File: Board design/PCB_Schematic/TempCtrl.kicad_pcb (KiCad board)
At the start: 4 copper layers, 80 x 100 mm, 164 parts, among them CON1 BARREL_JACK, IC1 ATMEGA328P-A, P1 233-2977, P2 820-8104, P3 RS485, P4 USB_OTG, P5 ICSP, P6 ADC breakout, SW1 DISABLE_COMMS, SW2 SWITCH_INV, U1 LM7805, U10 INA330, U11 ISO7242, U12 FT232RL, U13 ADS1262, U14 AD8639, U15 DAC8564, U16 AD8639, U17 DAC8564, U18 74LS125, U2 TMA0505S, U3 ADuM7642CRQZ, U4 ISO3088, U5 OPA548, U6 OPA548, U7 OPA548, U8 OPA548, U9 INA330, X1 TSX-3225 X1E0000210013

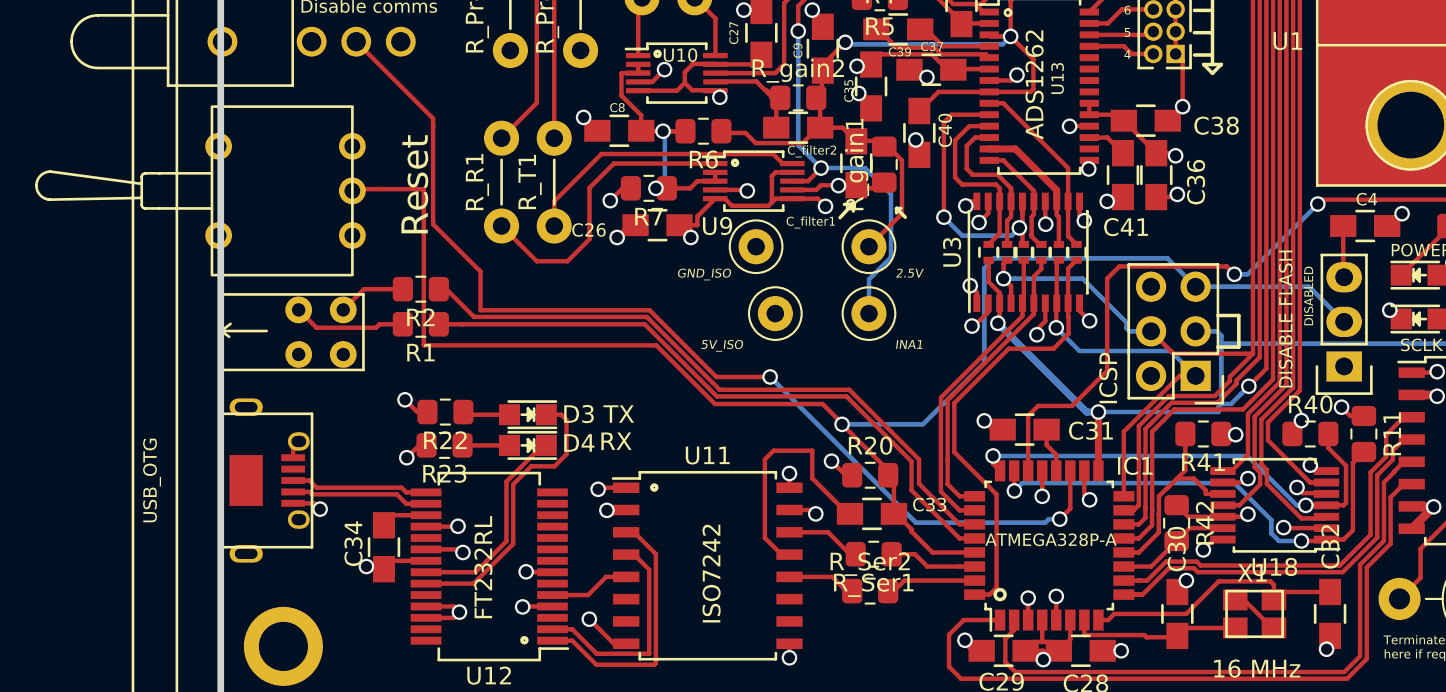
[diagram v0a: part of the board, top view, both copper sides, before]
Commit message: Schematic changes for v5
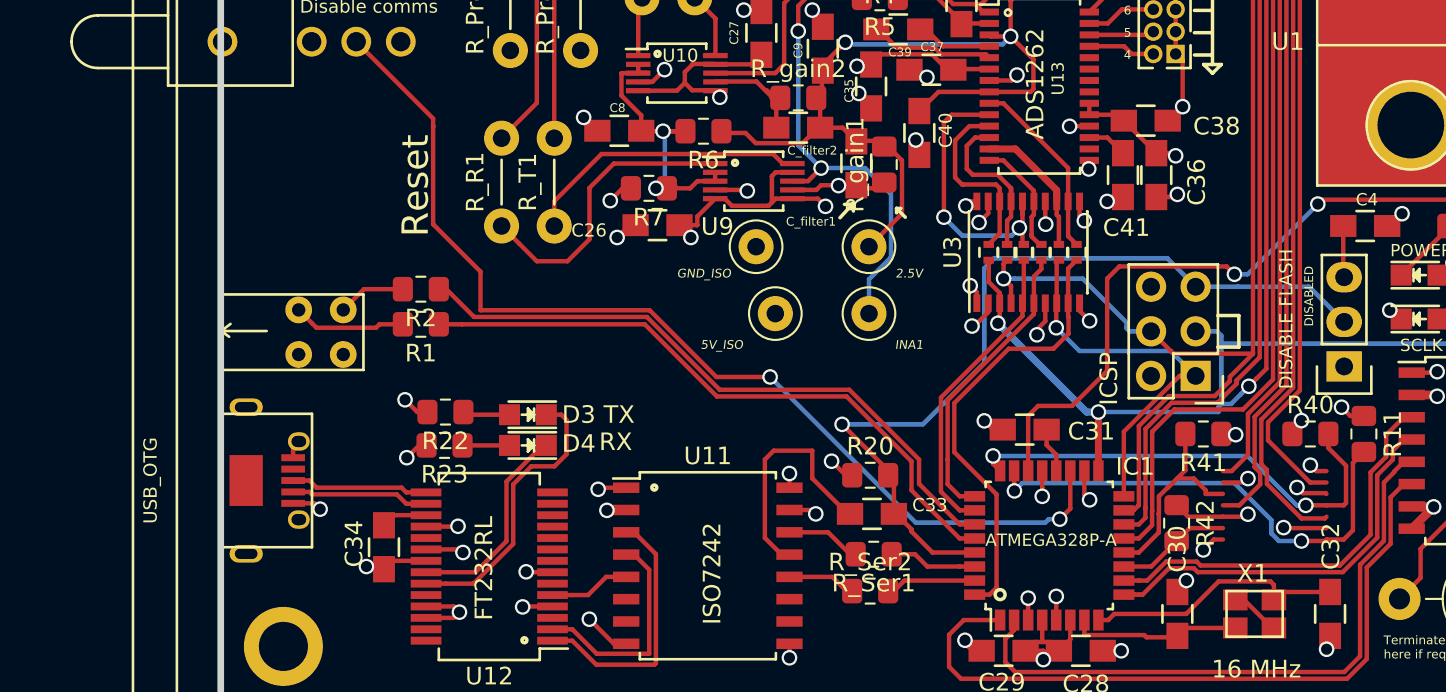
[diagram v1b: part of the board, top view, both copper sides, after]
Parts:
- removed SW2: SWITCH_INV, Custom:Toggle_Switch_819-9385
- removed U18: 74LS125, Package_SO:TSSOP-14_4.4x5mm_P0.65mm
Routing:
- net /ARD_RST: track 87.9 -> 49.1 mm

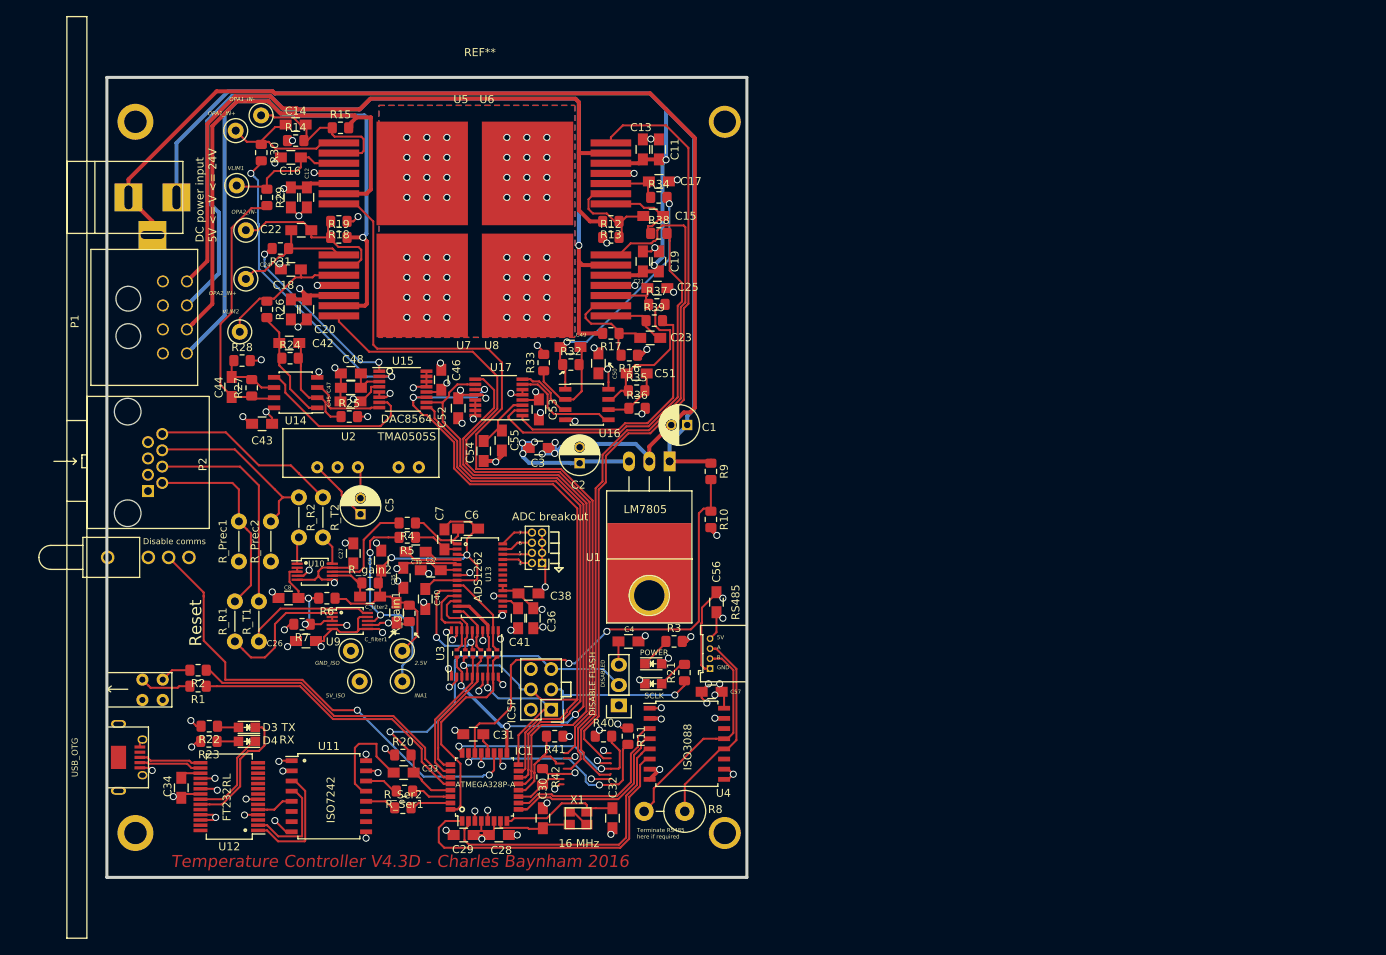
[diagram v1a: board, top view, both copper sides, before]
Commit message: Update schematic with v5 changes
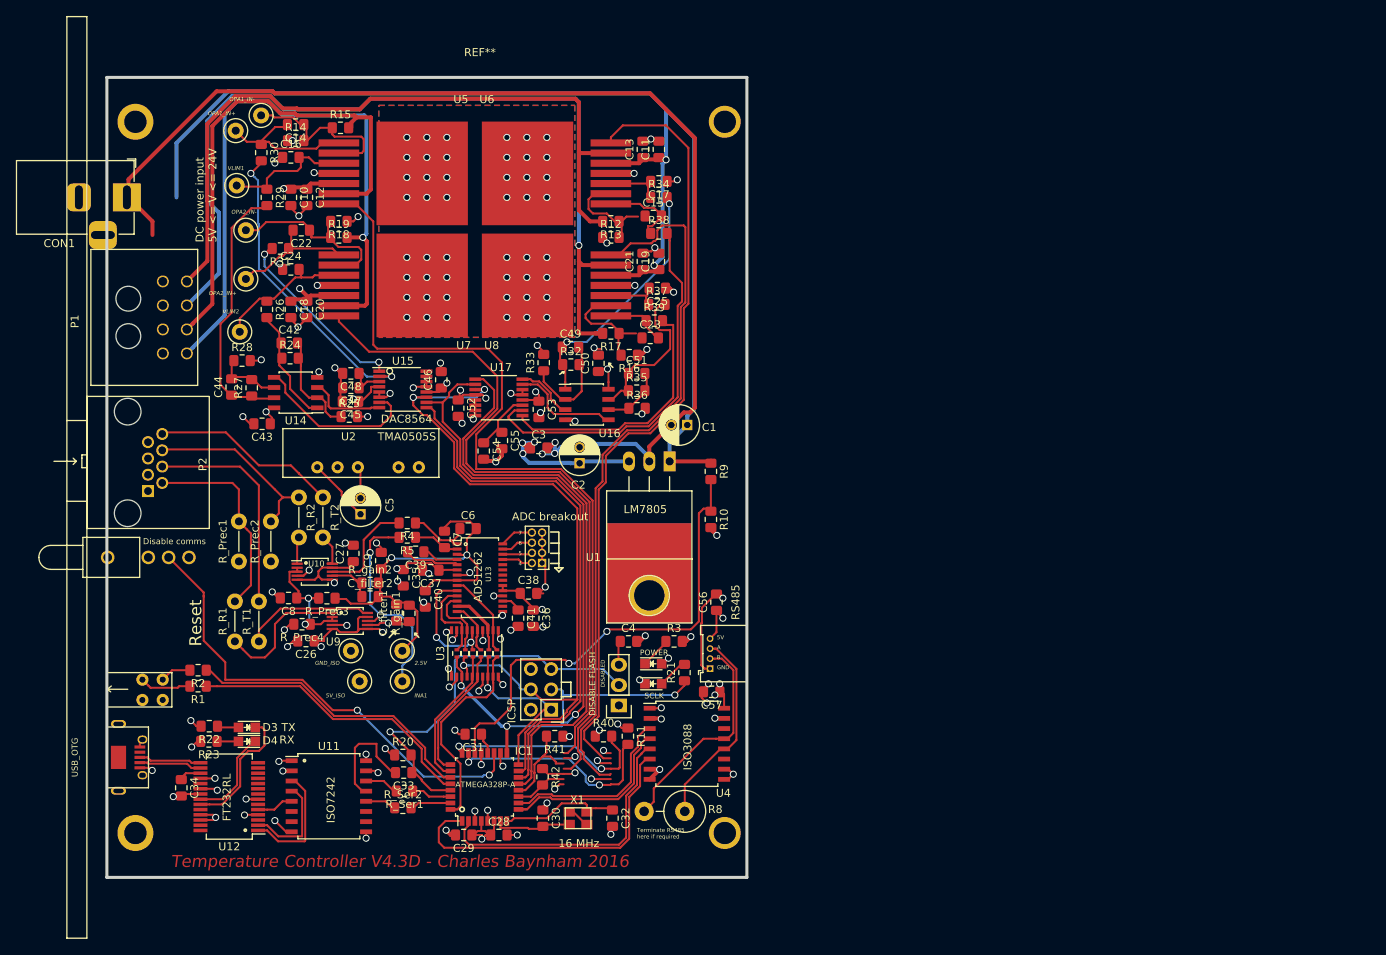
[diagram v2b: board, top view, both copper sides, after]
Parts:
- C10, C11, C12, C13, C14, C15, C16, C17, C18, C19, C20, C21, C22, C23, C24, C25, C26, C27, C28, C29, C3, C30, C31, C32, C33, C34, C35, C36, C37, C38, C39, C4, C40, C41, C42, C43, C44, C45, C46, C47, C48, C49, C50, C51, C52, C53, C54, C55, C56, C57, C6, C7, C8, C9, C_filter1, C_filter2: footprint Capacitors_SMD:C_0805_HandSoldering -> Capacitor_SMD:C_0805_2012Metric_Pad1.15x1.40mm_HandSolder
- CON1: footprint Connect:BARREL_JACK -> Connector_BarrelJack:BarrelJack_Horizontal
- R11, R40, R41, R42: value R_Small -> 10k
- R_gain1, R_gain2: value 24K -> 22k
- renumbered R6 to R_Prec3, R7 to R_Prec4
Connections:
- net /ADC_Chip/ADC_IN0 renamed /EXT_REF_P
- C6 pad 2: /ADC_2.5_REF -> /INA_2.5V_REF
- C7 pad 1: /ADC_2.5_REF -> /INA_2.5V_REF
- C9 pad 1: /ADC_2.5_REF -> /INA_2.5V_REF
- C_filter1 pad 2: /ADC_2.5_REF -> /INA_2.5V_REF
- C_filter2 pad 2: /ADC_2.5_REF -> /INA_2.5V_REF
- R_Prec3 pad 1: /ADC_2.5_REF -> /INA_2.5V_REF
- R_gain1 pad 2: /ADC_2.5_REF -> /INA_2.5V_REF
- R_gain2 pad 2: /ADC_2.5_REF -> /INA_2.5V_REF
- U13 pad 22: /ADC_Chip/ADC_IN1 -> /ANALOG_GND
- U13 pad 3: /ADC_2.5_REF -> /INA_2.5V_REF
- W3 pad 1: /ADC_2.5_REF -> /INA_2.5V_REF

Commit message: Pass PCB DRC with new footprint courtyards
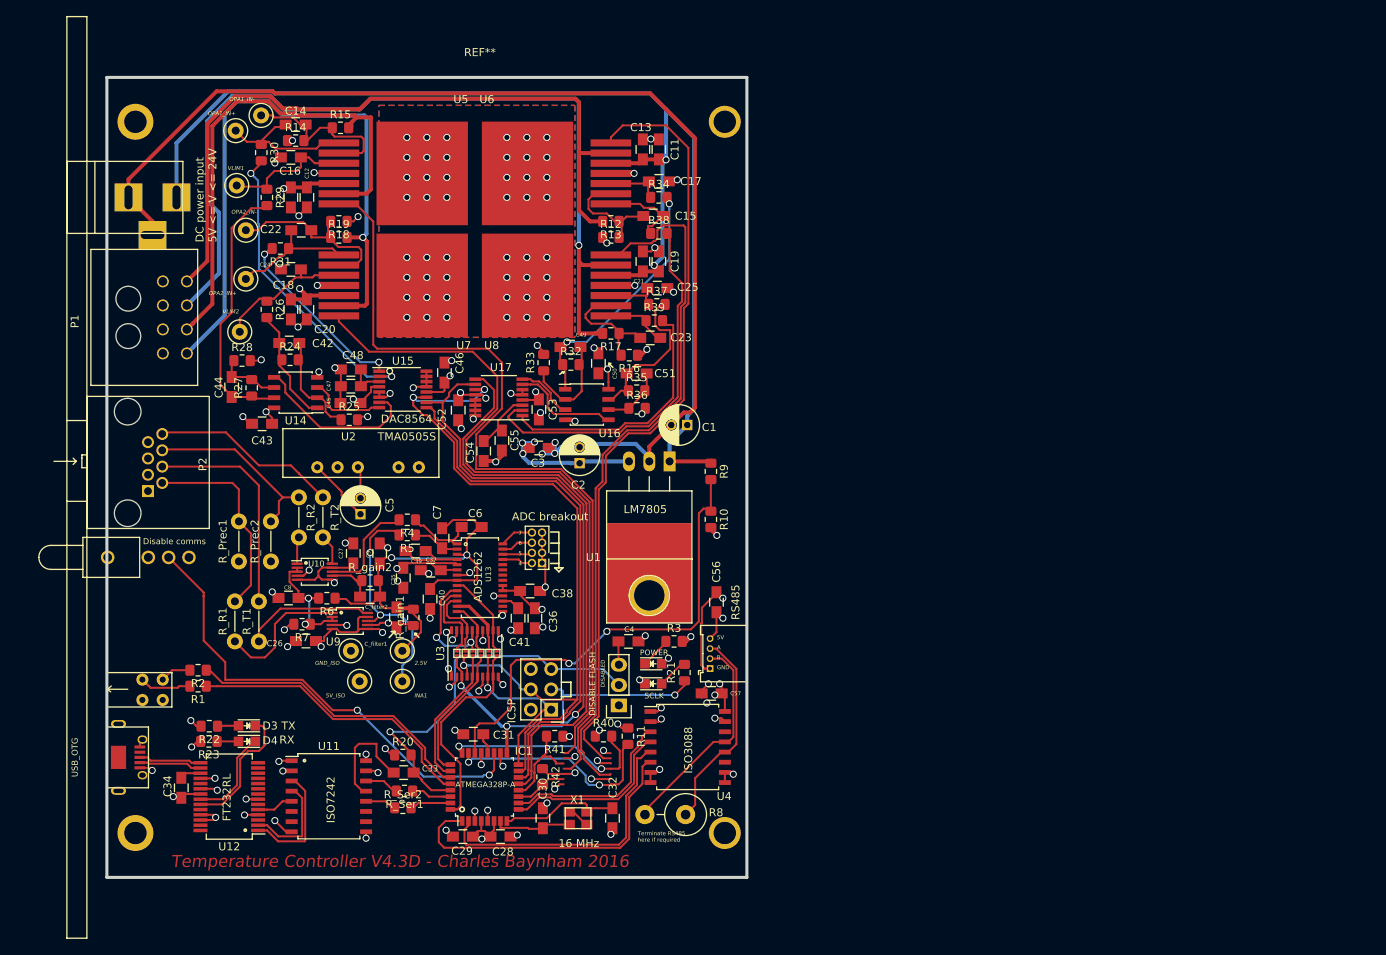
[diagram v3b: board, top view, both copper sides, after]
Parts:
- C10, C11, C12, C13, C14, C15, C16, C17, C18, C19, C20, C21, C22, C23, C24, C25, C26, C27, C28, C29, C3, C30, C31, C32, C33, C34, C35, C36, C37, C38, C39, C4, C40, C41, C42, C43, C44, C45, C46, C47, C48, C49, C50, C51, C52, C53, C54, C55, C56, C57, C6, C7, C8, C9, C_filter1, C_filter2: footprint Capacitor_SMD:C_0805_2012Metric_Pad1.15x1.40mm_HandSolder -> Capacitors_SMD:C_0805_HandSoldering
- CON1: footprint Connector_BarrelJack:BarrelJack_Horizontal -> Connect:BARREL_JACK
- JP2, JP3, JP4, JP5, JP6, JP7: footprint Resistors_SMD:R_0402 -> Custom:SmallJumperNoCourtyard
- R11, R40, R41, R42: value 10k -> R_Small
- R_gain1, R_gain2: value 22k -> 24K
- moved C46 0.98 mm to (207.2, 71.9)
- moved C9 0.92 mm to (199.1, 94.5)
- moved R_gain1 0.71 mm to (203.3, 102.5)
- moved C40 0.60 mm to (205.4, 100.2)
- moved C_filter1 0.57 mm to (201.2, 102.5)
- moved C48 0.50 mm to (195.5, 71.5)
- moved C6 0.49 mm to (210.6, 91.2)
- moved R8 0.41 mm to (237.3, 127.1)
- moved U4 0.41 mm to (237.6, 118.7)
- moved R4 0.40 mm to (202.6, 90.3)
- moved R25 0.40 mm to (195.3, 77.8)
- moved C38 0.36 mm to (217.9, 99.2)
- moved C7 0.34 mm to (206.9, 92.6)
- moved R5 0.30 mm to (202.6, 92.2)
- moved R_gain2 0.30 mm to (197.9, 97.9)
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- renumbered R_Prec3 to R6, R_Prec4 to R7
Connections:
- net /EXT_REF_P renamed /ADC_Chip/ADC_IN0
- C6 pad 2: /INA_2.5V_REF -> /ADC_2.5_REF
- C7 pad 1: /INA_2.5V_REF -> /ADC_2.5_REF
- C9 pad 1: /INA_2.5V_REF -> /ADC_2.5_REF
- C_filter1 pad 2: /INA_2.5V_REF -> /ADC_2.5_REF
- C_filter2 pad 2: /INA_2.5V_REF -> /ADC_2.5_REF
- R6 pad 1: /INA_2.5V_REF -> /ADC_2.5_REF
- R_gain1 pad 2: /INA_2.5V_REF -> /ADC_2.5_REF
- R_gain2 pad 2: /INA_2.5V_REF -> /ADC_2.5_REF
- U13 pad 22: /ANALOG_GND -> /ADC_Chip/ADC_IN1
- U13 pad 3: /INA_2.5V_REF -> /ADC_2.5_REF
- W3 pad 1: /INA_2.5V_REF -> /ADC_2.5_REF
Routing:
- net /ADC_2.5_REF: track 53.8 -> 56.6 mm
- net /RS485_GND: track 20.7 -> 18.2 mm
- net +5V: track 61.2 -> 62.7 mm
- net /INA_ERROR_1: track 27.1 -> 28.3 mm
- net /RS485_B: track 28.0 -> 26.9 mm
- net Earth_Clean: track 247.7 -> 248.7 mm
- net /ADC_CS_ISO: track 16.5 -> 15.9 mm
- net /MOSI: track 97.6 -> 98.1 mm
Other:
- board text removed: "Reset"
